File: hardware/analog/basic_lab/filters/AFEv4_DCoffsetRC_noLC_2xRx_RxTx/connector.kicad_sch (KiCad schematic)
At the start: 2 parts

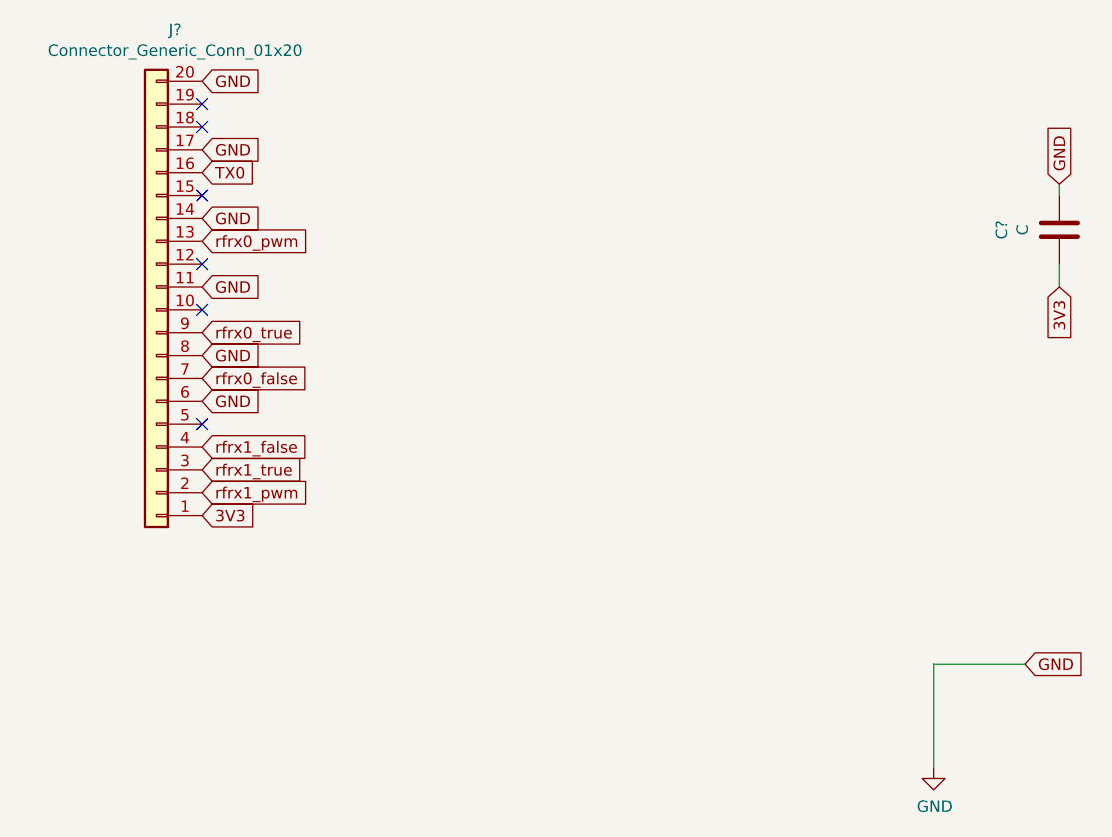
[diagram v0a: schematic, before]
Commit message: started 2xRx / RxTx PCBs with no / simple LC filters
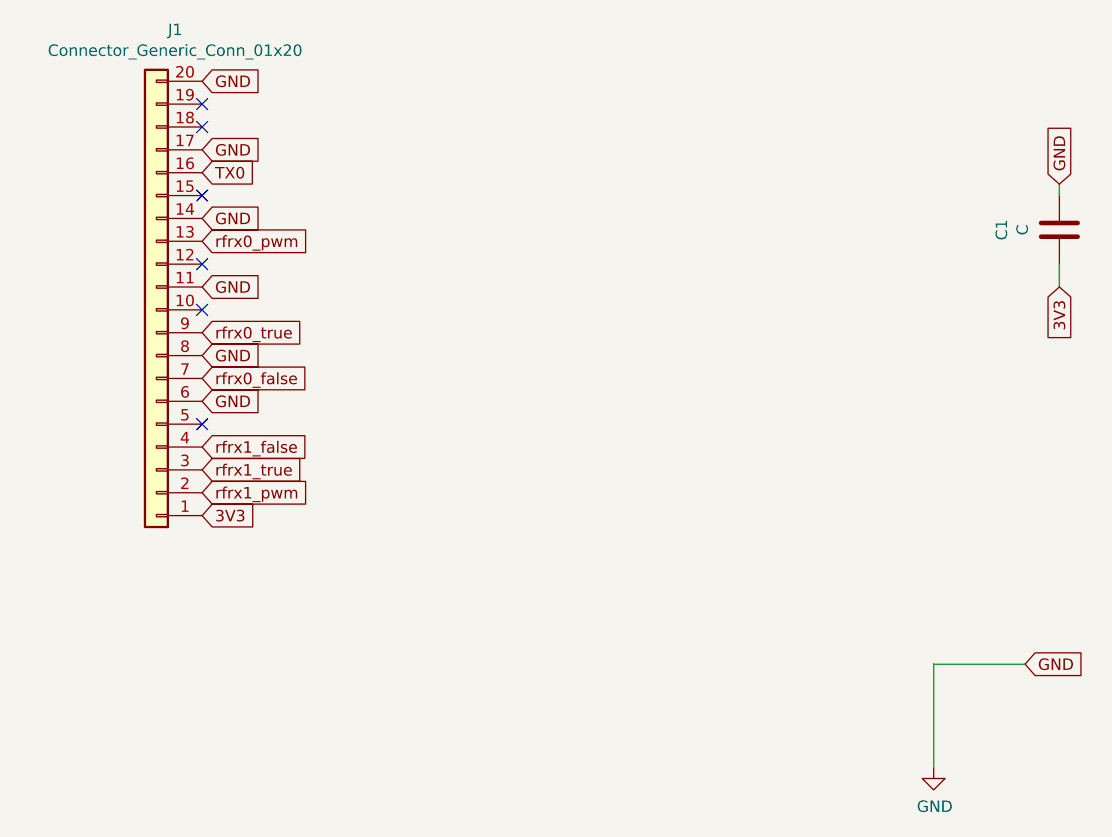
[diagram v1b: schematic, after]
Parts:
- gave numbers to parts that had none: 2
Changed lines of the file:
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@@
   (symbol (lib_id "power:GND") (at 140.97 128.27 0) (unit 1)
     (in_bom yes) (on_board yes)
-    (property "Reference" "#PWR?" (id 0) (at 140.97 134.62 0)
+    (property "Reference" "#PWR01" (id 0) (at 140.97 134.62 0)
       (effects (font (size 1.27 1.27)) hide)
     )
@@
   (symbol (lib_id "bgt:Connector_Generic_Conn_01x20") (at 54.61 77.47 180) (unit 1)
     (in_bom yes) (on_board yes)
-    (property "Reference" "J?" (id 0) (at 56.6928 46.355 0))
+    (property "Reference" "J1" (id 0) (at 56.6928 46.355 0))
     (property "Value" "Connector_Generic_Conn_01x20" (id 1) (at 56.6928 48.6664 0))
     (property "Footprint" "Connector_PinHeader_2.54mm:PinHeader_1x20_P2.54mm_Vertical" (id 2) (at 54.61 77.47 0)
@@
   (symbol (lib_id "Device:C") (at 154.94 68.58 0) (unit 1)
     (in_bom yes) (on_board yes)
-    (property "Reference" "C?" (id 0) (at 148.5392 68.58 90))
+    (property "Reference" "C1" (id 0) (at 148.5392 68.58 90))
     (property "Value" "C" (id 1) (at 150.8506 68.58 90))
     (property "Footprint" "Capacitor_THT:C_Axial_L3.8mm_D2.6mm_P7.50mm_Horizontal" (id 2) (at 155.9052 72.39 0)

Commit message: started 2xRx / RxTx PCBs with no / simple LC filters: Gerber with THT board; started SMD board in the same DIR
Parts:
- C1: footprint Capacitor_THT:C_Axial_L3.8mm_D2.6mm_P7.50mm_Horizontal -> Capacitor_SMD:C_1206_3216Metric
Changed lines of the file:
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@@
     (property "Reference" "C1" (id 0) (at 148.5392 68.58 90))
     (property "Value" "C" (id 1) (at 150.8506 68.58 90))
-    (property "Footprint" "Capacitor_THT:C_Axial_L3.8mm_D2.6mm_P7.50mm_Horizontal" (id 2) (at 155.9052 72.39 0)
+    (property "Footprint" "Capacitor_SMD:C_1206_3216Metric" (id 2) (at 155.9052 72.39 0)
       (effects (font (size 1.27 1.27)) hide)
     )

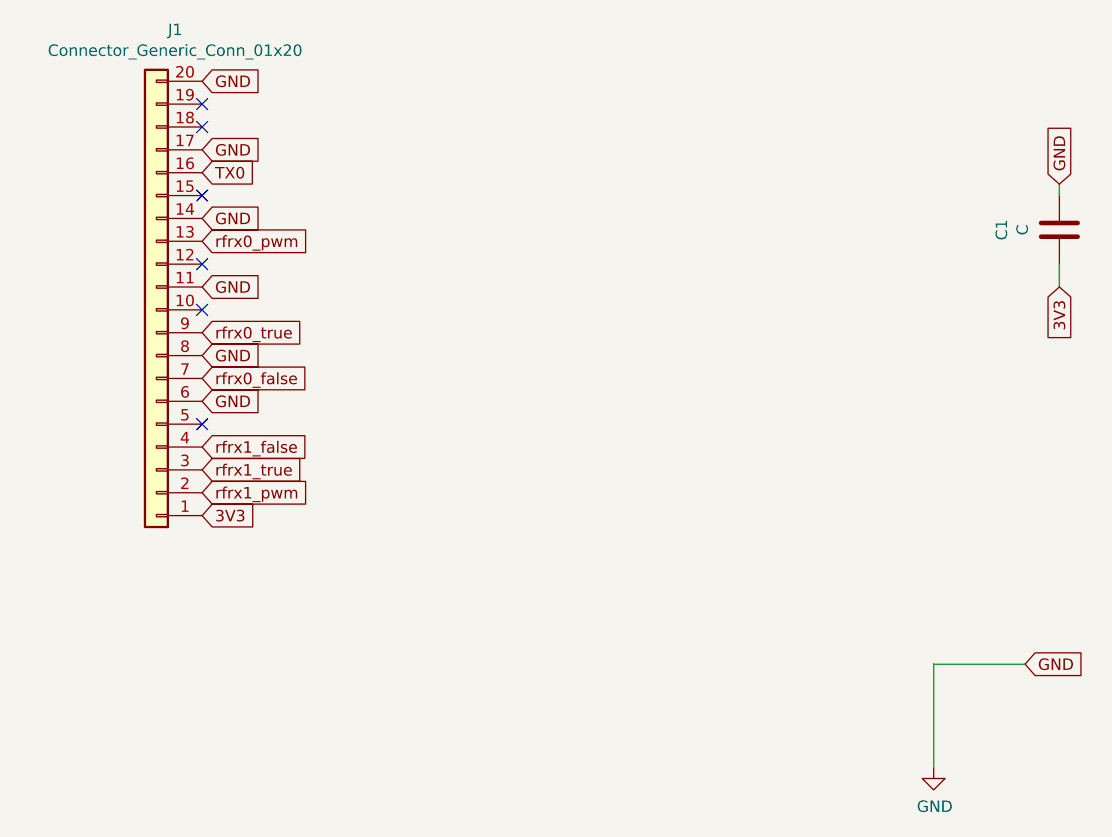
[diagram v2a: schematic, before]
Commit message: started phase DSP: DC POWER filter for AFE
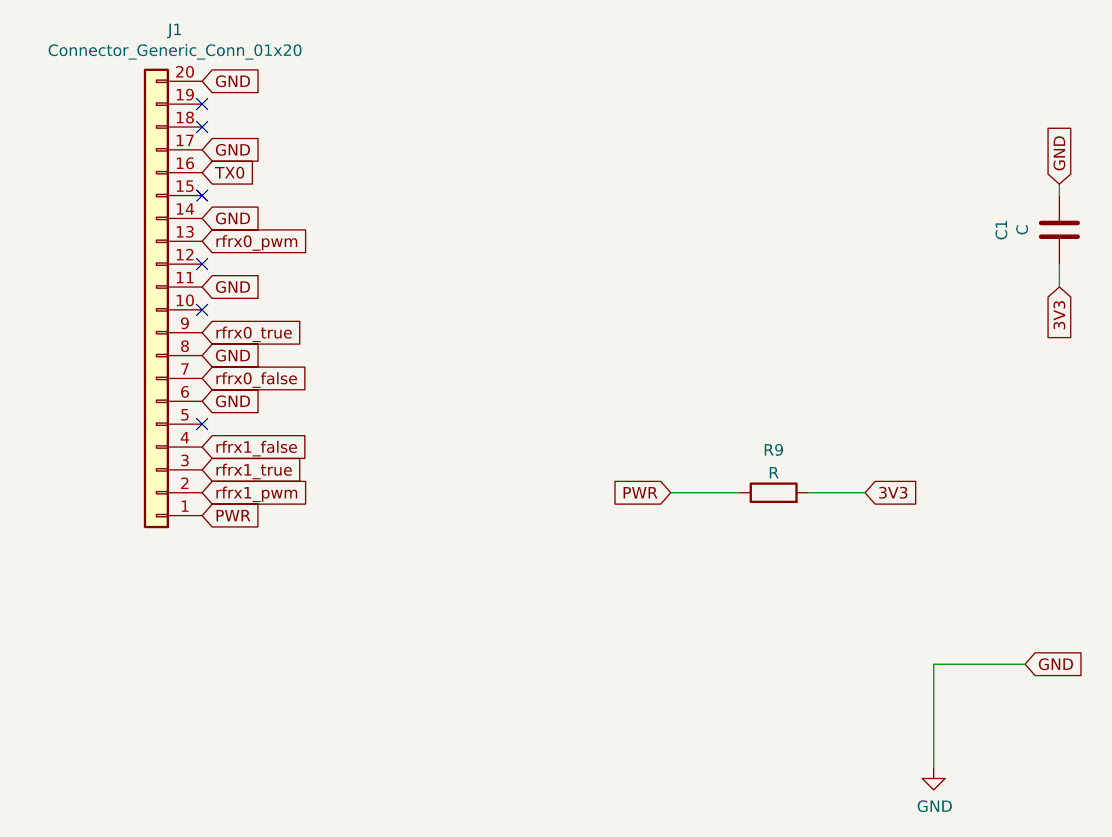
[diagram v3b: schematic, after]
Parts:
- added R9: R, Resistor_SMD:R_0805_2012Metric, symbol Device:R
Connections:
- net 3V3: now also R9.2; no longer J1.1 (Pin_1)
- new net PWR: J1.1 (Pin_1), R9.1
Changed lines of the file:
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@@
+    (stroke (width 0) (type default) (color 0 0 0 0))
+  )
+  (wire (pts (xy 127 97.79) (xy 133.35 97.79))
+    (stroke (width 0) (type default) (color 0 0 0 0))
+  )
+  (wire (pts (xy 111.76 97.79) (xy 119.38 97.79))
     (stroke (width 0) (type default) (color 0 0 0 0))
   )
@@
     )
   )
-  (global_label "3V3" (shape input) (at 59.69 100.33 0) (fields_autoplaced)
+  (global_label "3V3" (shape input) (at 133.35 97.79 0) (fields_autoplaced)
     (effects (font (size 1.27 1.27)) (justify left))
-    (property "Intersheet References" "${INTERSHEET_REFS}" (id 0) (at 13.97 -5.08 0)
+    (property "Intersheet References" "${INTERSHEET_REFS}" (id 0) (at 87.63 -7.62 0)
       (effects (font (size 1.27 1.27)) hide)
+    )
+  )
+  (global_label "PWR" (shape input) (at 111.76 97.79 180) (fields_autoplaced)
+    (effects (font (size 1.27 1.27)) (justify right))
+    (property "Intersheet References" "${INTERSHEET_REFS}" (id 0) (at 105.4444 97.7106 0)
+      (effects (font (size 1.27 1.27)) (justify right) hide)
     )
   )
@@
     )
   )
+  (global_label "PWR" (shape input) (at 59.69 100.33 0) (fields_autoplaced)
+    (effects (font (size 1.27 1.27)) (justify left))
+    (property "Intersheet References" "${INTERSHEET_REFS}" (id 0) (at 66.0056 100.2506 0)
+      (effects (font (size 1.27 1.27)) (justify left) hide)
+    )
+  )
   (global_label "GND" (shape input) (at 59.69 74.93 0) (fields_autoplaced)
     (effects (font (size 1.27 1.27)) (justify left))
@@
     (pin "1")
   )
+  (symbol (lib_id "Device:R") (at 123.19 97.79 90) (unit 1)
+    (in_bom yes) (on_board yes) (fields_autoplaced)
+    (property "Reference" "R9" (id 0) (at 123.19 93.0742 90))
+    (property "Value" "R" (id 1) (at 123.19 95.6111 90))
+    (property "Footprint" "Resistor_SMD:R_0805_2012Metric" (id 2) (at 123.19 99.568 90)
+      (effects (font (size 1.27 1.27)) hide)
+    )
+    (property "Datasheet" "~" (id 3) (at 123.19 97.79 0)
+      (effects (font (size 1.27 1.27)) hide)
+    )
+    (pin "1")
+    (pin "2")
+  )
   (symbol (lib_id "bgt:Connector_Generic_Conn_01x20") (at 54.61 77.47 180) (unit 1)
